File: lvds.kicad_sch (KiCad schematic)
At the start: 97 parts, among them J15 Conn_FFC_Amphenol_62684-40210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

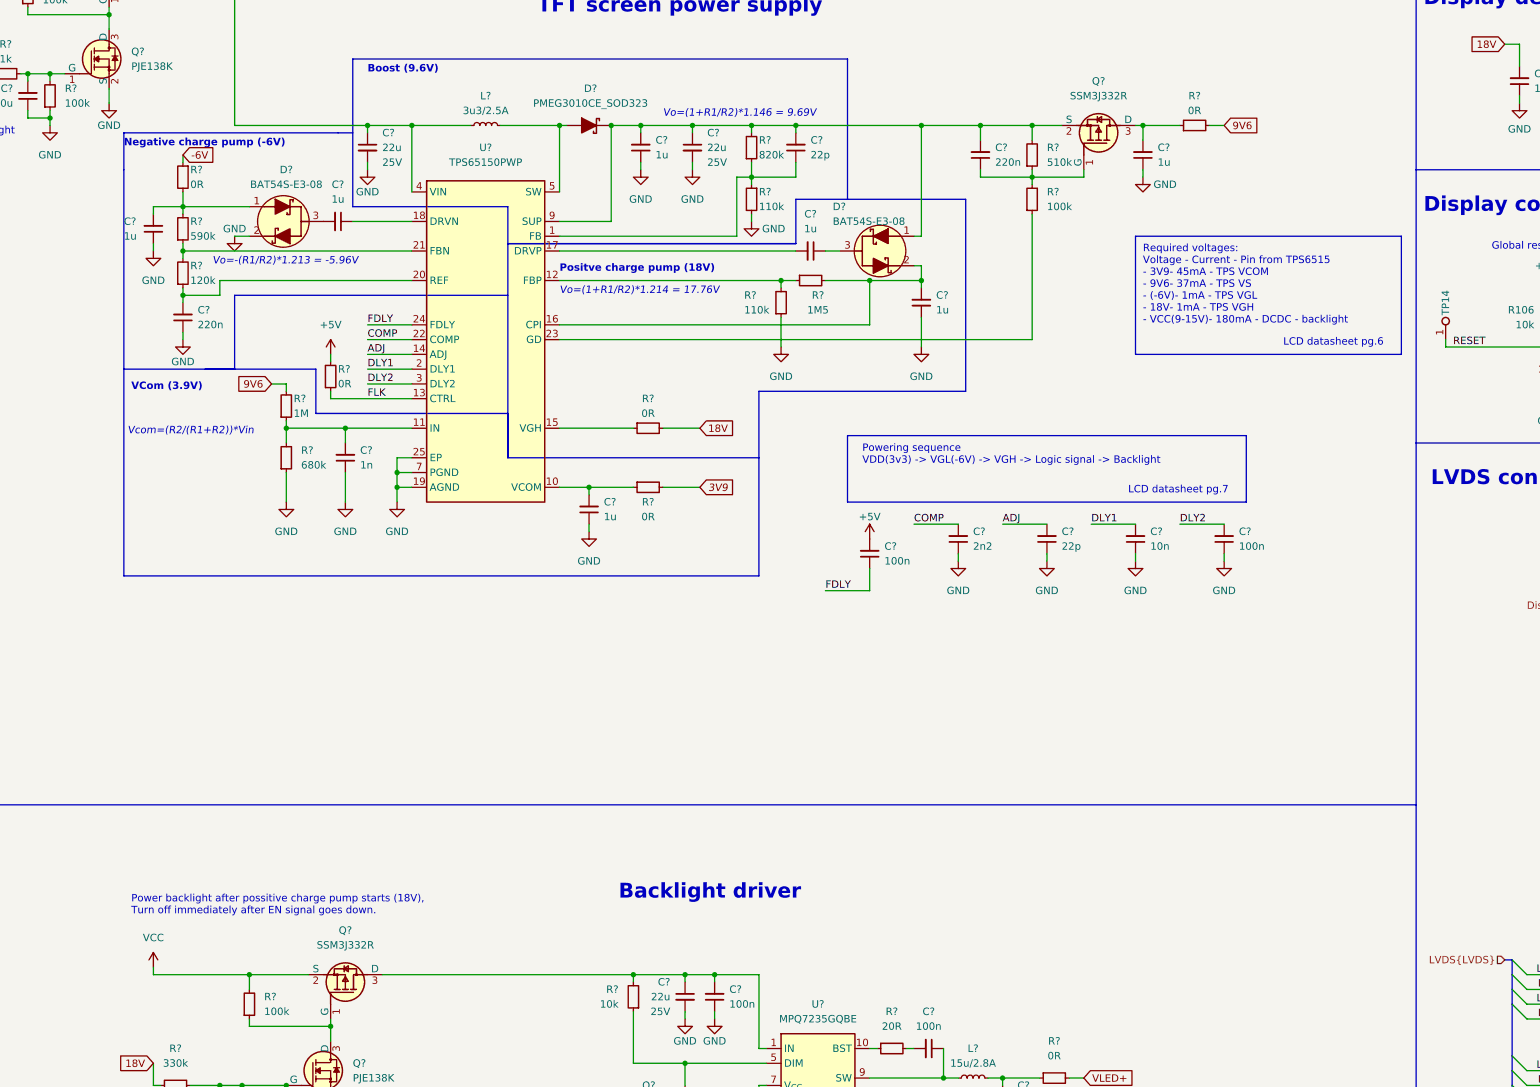
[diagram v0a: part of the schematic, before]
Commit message: [#54932] Change power supply to output voltage for backlight
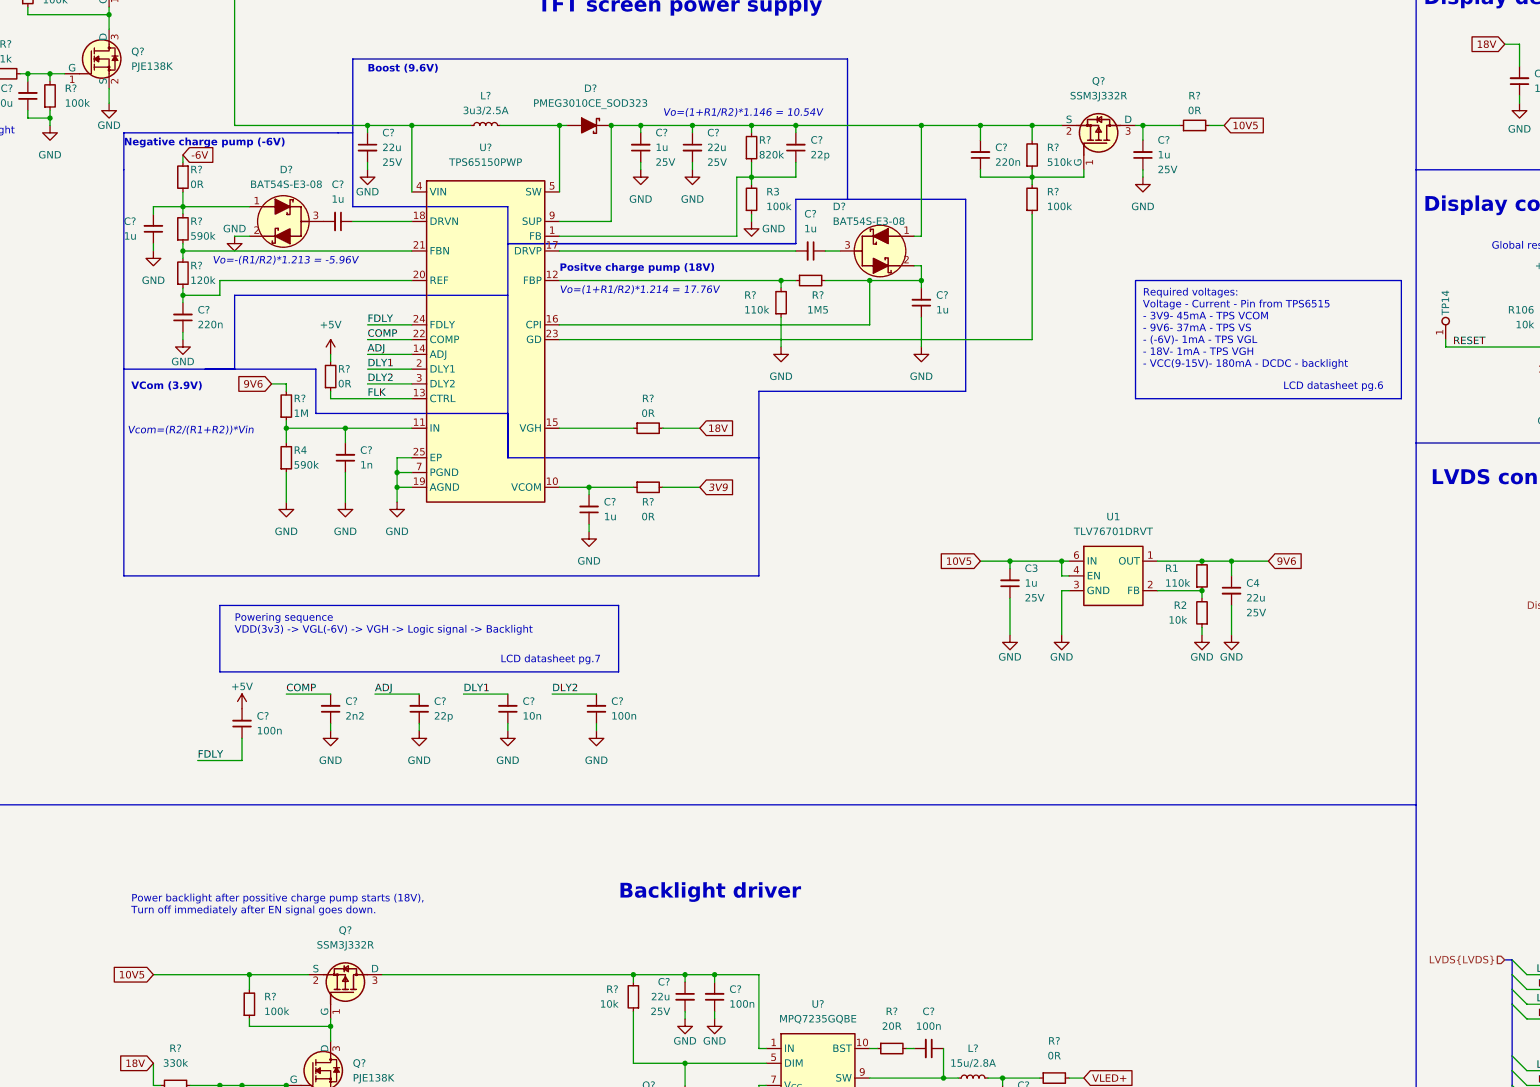
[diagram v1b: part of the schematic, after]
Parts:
- removed R?: R_680k_0402, antmicro-footprints:R_0402_1005Metric, symbol antmicroResistors0402:R_680k_0402
- removed R?: R_110k_0402, antmicro-footprints:R_0402_1005Metric, symbol antmicroResistors0402:R_110k_0402
- added C3: C_1u_25V_0402, antmicro-footprints:C_0402_1005Metric, symbol antmicroCapacitors0402:C_1u_25V_0402
- added C4: C_22u_25V_0805, antmicro-footprints:C_0805_2012Metric, symbol antmicroCapacitorsmisc:C_22u_25V_0805
- added R1: R_110k_0402, antmicro-footprints:R_0402_1005Metric, symbol antmicroResistors0402:R_110k_0402
- added R2: R_10k_0402, antmicro-footprints:R_0402_1005Metric, symbol antmicroResistors0402:R_10k_0402
- added R3: R_100k_0402, antmicro-footprints:R_0402_1005Metric, symbol antmicroResistors0402:R_100k_0402
- added R4: R_590k_0402, antmicro-footprints:R_0402_1005Metric, symbol antmicroResistors0402:R_590k_0402
- added U1: TLV76701_WSON6, antmicro-footprints:WSON-6-1EP_2x2mm_P0.65mm, symbol antmicroPMICVoltageRegulatorsLinear:TLV76701_WSON6
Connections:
- net 9V6: now also C4.1, R1.2, U1.1 (OUT); no longer R?.2
- net GND: now also C3.1, C4.2, R2.1, R3.1, R4.1, U1.3 (GND), U1.5 (GND), U1.7 (PAD)
- net at C?.2, R?.1, U?.11 (IN): now also R4.2
- net at C?.1, R?.1, U?.1 (FB): now also R3.2
- net VCC renamed 10V5
- net 10V5: now also R?.2, C3.2, U1.4 (EN), U1.6 (IN)
- new net: R1.1, R2.2, U1.2 (FB)
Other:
- note added: "Vo=(1+R1/R2)*1.146 = 10.54V"
- note removed: "Vo=(1+R1/R2)*1.146 = 9.69V"
- moved on the sheet: C?

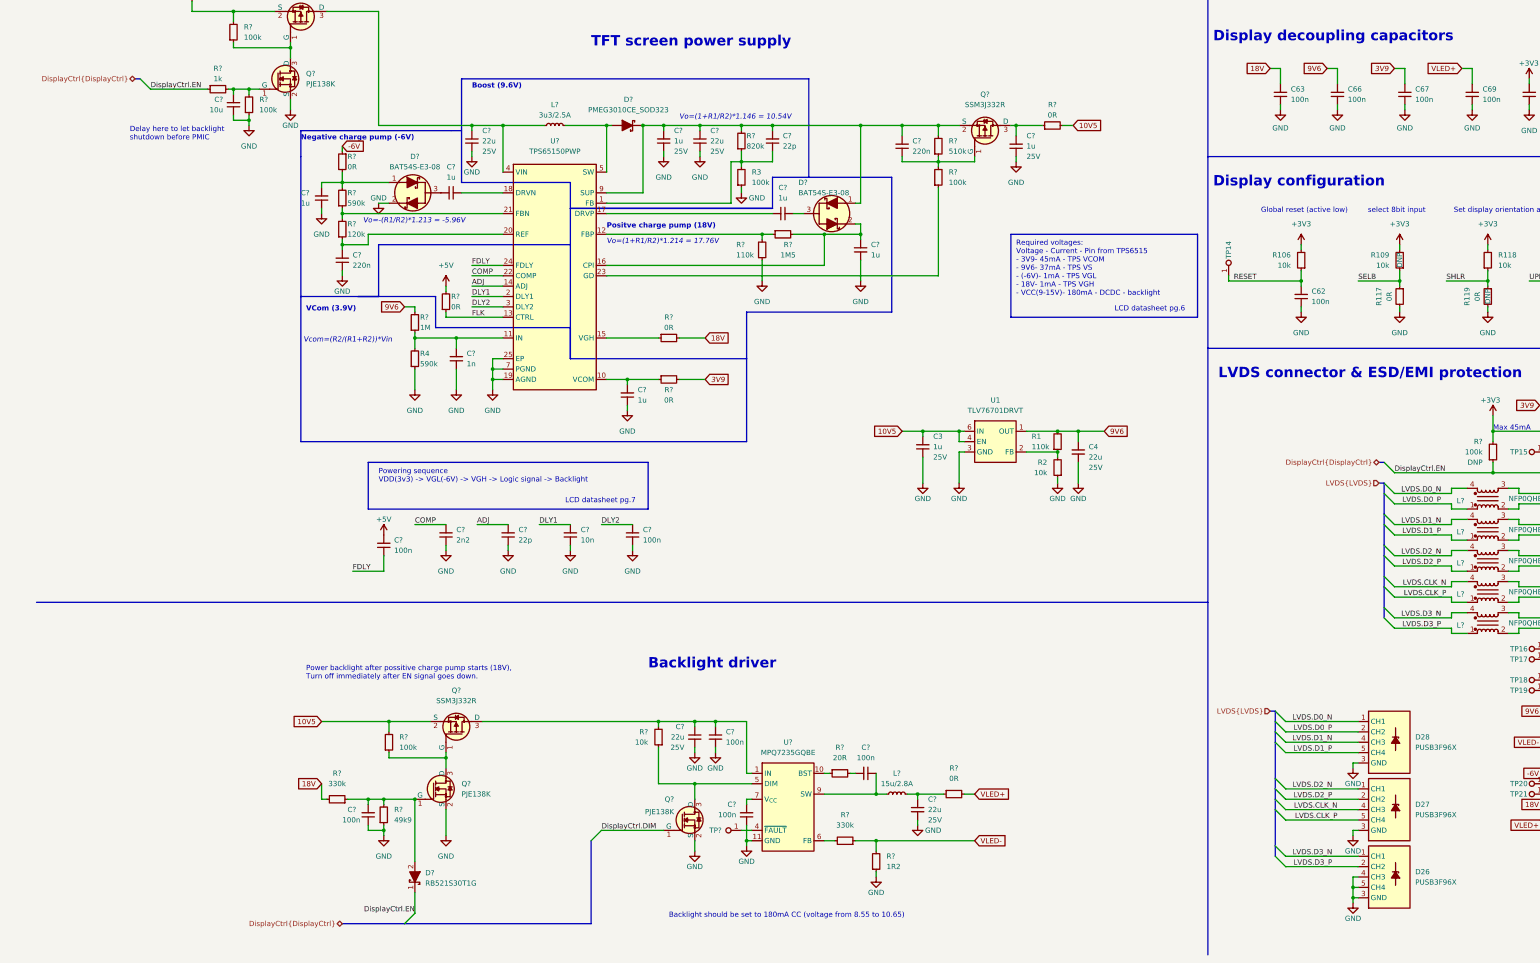
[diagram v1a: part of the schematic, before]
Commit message: [#54932] Remove DSI conn; Add AntmUD conn; Rename buses
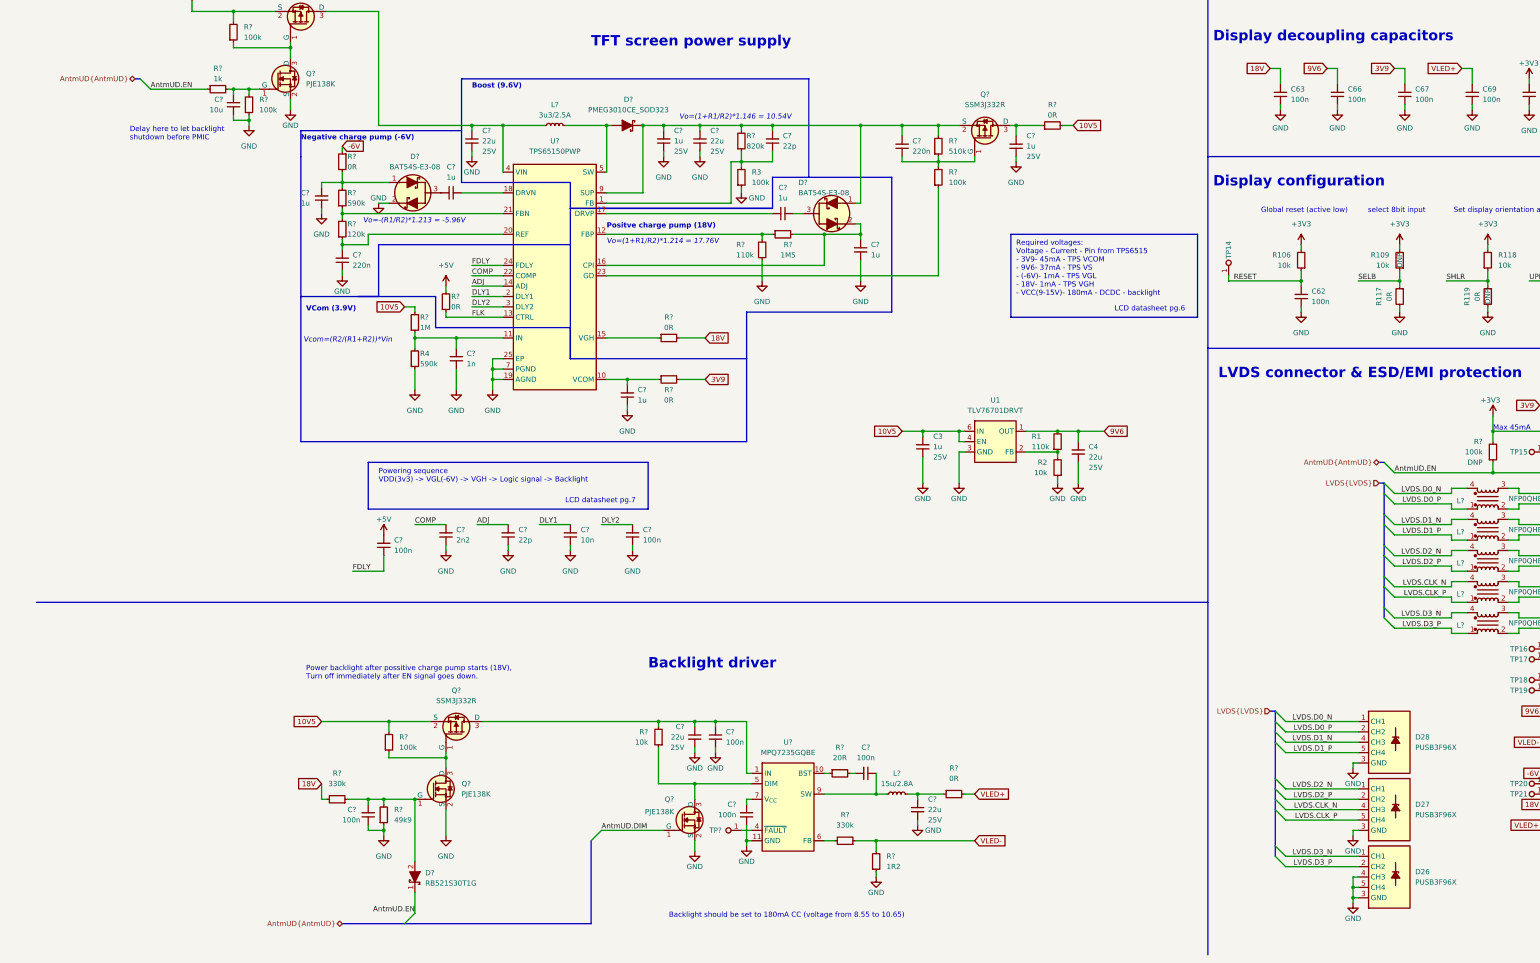
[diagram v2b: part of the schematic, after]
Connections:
- net 10V5: now also R?.2
- net 9V6: no longer R?.2
- net DisplayCtrl.DIM renamed AntmUD.DIM
- net DisplayCtrl.EN renamed AntmUD.EN
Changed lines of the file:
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@@
     (effects (font (size 1.27 1.27)) (justify left bottom))
   )
-  (label "DisplayCtrl.DIM" (at 151.13 222.25 0) (fields_autoplaced)
-    (effects (font (size 1.27 1.27)) (justify left bottom))
-  )
-  (label "DisplayCtrl.EN" (at 345.44 134.62 0) (fields_autoplaced)
+  (label "AntmUD.DIM" (at 151.13 222.25 0) (fields_autoplaced)
+    (effects (font (size 1.27 1.27)) (justify left bottom))
+  )
+  (label "AntmUD.EN" (at 345.44 134.62 0) (fields_autoplaced)
     (effects (font (size 1.27 1.27)) (justify left bottom))
   )
@@
     (effects (font (size 1.27 1.27)) (justify left bottom))
   )
-  (label "DisplayCtrl.EN" (at 105.41 242.57 180) (fields_autoplaced)
+  (label "AntmUD.EN" (at 105.41 242.57 180) (fields_autoplaced)
     (effects (font (size 1.27 1.27)) (justify right bottom))
   )
@@
     (effects (font (size 1.27 1.27)) (justify right bottom))
   )
-  (label "DisplayCtrl.EN" (at 40.64 40.64 0) (fields_autoplaced)
+  (label "AntmUD.EN" (at 40.64 40.64 0) (fields_autoplaced)
     (effects (font (size 1.27 1.27)) (justify left bottom))
   )
@@
     )
   )
-  (global_label "9V6" (shape input) (at 102.87 93.98 180) (fields_autoplaced)
-    (effects (font (size 1.27 1.27)) (justify right))
-    (property "Intersheetrefs" "${INTERSHEET_REFS}" (at 97.0382 93.9006 0)
-      (effects (font (size 1.27 1.27)) (justify right) hide)
-    )
-  )
   (global_label "VLED+" (shape input) (at 361.95 35.56 180) (fields_autoplaced)
     (effects (font (size 1.27 1.27)) (justify right))
@@
     )
   )
+  (global_label "10V5" (shape input) (at 102.87 93.98 180) (fields_autoplaced)
+    (effects (font (size 1.27 1.27)) (justify right))
+    (property "Intersheetrefs" "${INTERSHEET_REFS}" (at 95.8219 93.98 0)
+      (effects (font (size 1.27 1.27)) (justify right) hide)
+    )
+  )
   (global_label "18V" (shape input) (at 176.53 101.6 0) (fields_autoplaced)
     (effects (font (size 1.27 1.27)) (justify left))
@@
     )
   )
-  (hierarchical_label "DisplayCtrl{DisplayCtrl}" (shape bidirectional) (at 87.63 245.11 180) (fields_autoplaced)
+  (hierarchical_label "AntmUD{AntmUD}" (shape bidirectional) (at 36.83 38.1 180) (fields_autoplaced)
+    (effects (font (size 1.27 1.27)) (justify right))
+  )
+  (hierarchical_label "AntmUD{AntmUD}" (shape bidirectional) (at 341.63 132.08 180) (fields_autoplaced)
+    (effects (font (size 1.27 1.27)) (justify right))
+  )
+  (hierarchical_label "AntmUD{AntmUD}" (shape bidirectional) (at 87.63 245.11 180) (fields_autoplaced)
     (effects (font (size 1.27 1.27)) (justify right))
   )
@@
     (effects (font (size 1.27 1.27)) (justify right))
   )
-  (hierarchical_label "DisplayCtrl{DisplayCtrl}" (shape bidirectional) (at 36.83 38.1 180) (fields_autoplaced)
-    (effects (font (size 1.27 1.27)) (justify right))
-  )
-  (hierarchical_label "DisplayCtrl{DisplayCtrl}" (shape bidirectional) (at 341.63 132.08 180) (fields_autoplaced)
-    (effects (font (size 1.27 1.27)) (justify right))
-  )
